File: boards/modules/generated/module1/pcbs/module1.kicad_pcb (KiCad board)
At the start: 2 copper layers, 75.2 x 75.2 mm, 19 parts

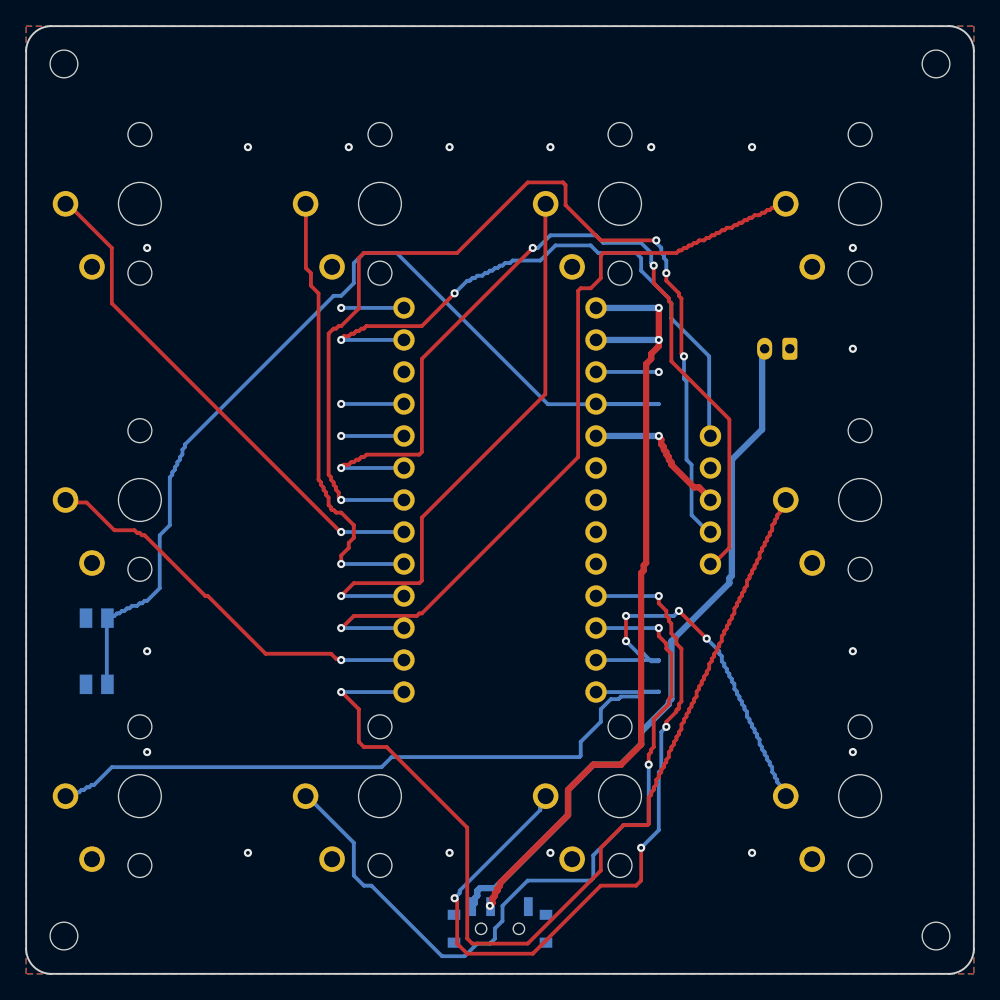
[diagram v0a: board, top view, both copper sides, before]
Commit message: Regenerate twelve-key module 1 PCB exports and underside-display previews
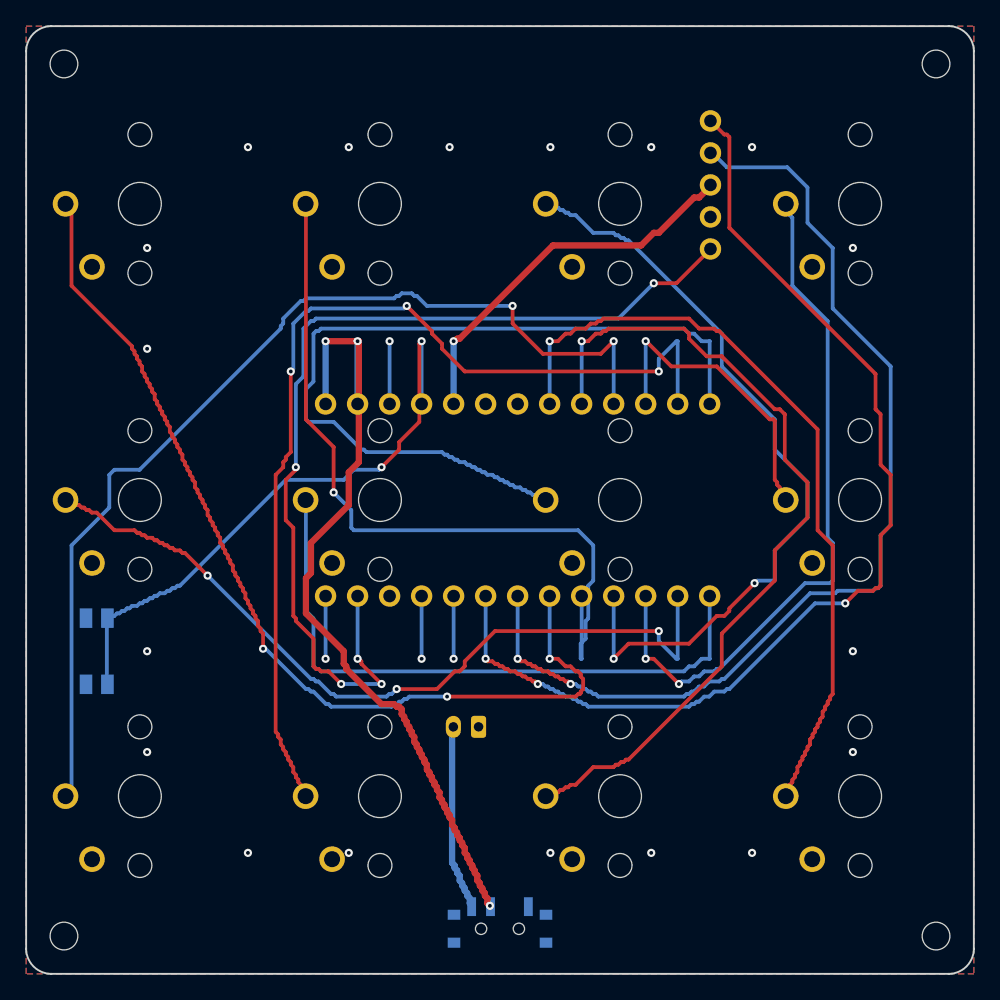
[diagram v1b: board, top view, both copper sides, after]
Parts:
- added S11: , switch_choc_v1_v2, F.Cu at (109.5, 123.5)
- added S12: , switch_choc_v1_v2, F.Cu at (128.6, 123.5)
- DISP1: moved to B.Cu
- moved S7 44.8 mm to (109.5, 100.0)
- moved S8 44.8 mm to (128.6, 100.0)
- moved JST1 38.9 mm to (97.3, 118.0)
- moved S9 38.1 mm to (71.4, 123.5)
- moved S10 38.1 mm to (90.5, 123.5)
- moved S6 38.1 mm to (90.5, 100.0)
- moved DISP1 25.0 mm to (100.0, 75.0)
- moved MCU1 1.40 mm to (101.4, 100.0), turned to 90 degrees
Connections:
- DISP1 pad 1: DISPLAY_MOSI -> DISPLAY_CS
- DISP1 pad 2: DISPLAY_SCK -> GND
- DISP1 pad 4: GND -> DISPLAY_SCK
- DISP1 pad 5: DISPLAY_CS -> DISPLAY_MOSI
- MCU1 pad 10: key_r3_c2 -> key_r2_c4
- MCU1 pad 11: key_r3_c4 -> key_r3_c2
- MCU1 pad 12: key_r3_c1 -> key_r2_c3
- MCU1 pad 13: key_r2_c4 -> key_r2_c2
- MCU1 pad 7: P19 -> key_r3_c4
- MCU1 pad 8: P18 -> key_r3_c3
- MCU1 pad 9: key_r3_c3 -> key_r3_c1
- S10 pad 2: key_r3_c4 -> key_r3_c2
- S6 pad 2: key_r2_c4 -> key_r2_c2
- S7 pad 2: key_r3_c1 -> key_r2_c3
- S8 pad 2: key_r3_c2 -> key_r2_c4
- S9 pad 2: key_r3_c3 -> key_r3_c1
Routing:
- net key_r2_c3: track 0.00 -> 65.7 mm
- net key_r2_c4: track 79.6 -> 24.5 mm
- net key_r2_c2: track 0.00 -> 50.5 mm
- net BAT_P: track 55.9 -> 15.0 mm
- net key_r1_c1: track 40.4 -> 79.2 mm, vias 1 -> 3
- net key_r2_c1: track 32.3 -> 63.8 mm, vias 1 -> 3
- net RST: track 77.6 -> 48.5 mm, vias 0 -> 2
- net key_r3_c4: track 33.1 -> 62.0 mm, vias 4 -> 1
- net DISPLAY_CS: track 49.0 -> 77.3 mm, vias 2 -> 5
- net key_r1_c2: track 36.1 -> 61.6 mm
- net key_r3_c1: track 56.8 -> 81.7 mm, vias 0 -> 2
- net 3V3: track 12.1 -> 30.7 mm
- net key_r3_c2: track 62.3 -> 79.4 mm, vias 2 -> 3
- net key_r1_c3: track 46.1 -> 62.3 mm, vias 1 -> 2
- net DISPLAY_MOSI: track 70.2 -> 85.3 mm
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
